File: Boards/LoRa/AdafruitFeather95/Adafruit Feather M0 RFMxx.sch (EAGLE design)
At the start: 38 parts, among them SW1 SPST_TACT-KMR2, U2 AP2112K-3.3, U3 MCP73831T-2ACI/OT, U4 RFM69HCW, X1 JSTPH, X2 32.768, X3 microUSB, X4 uFL

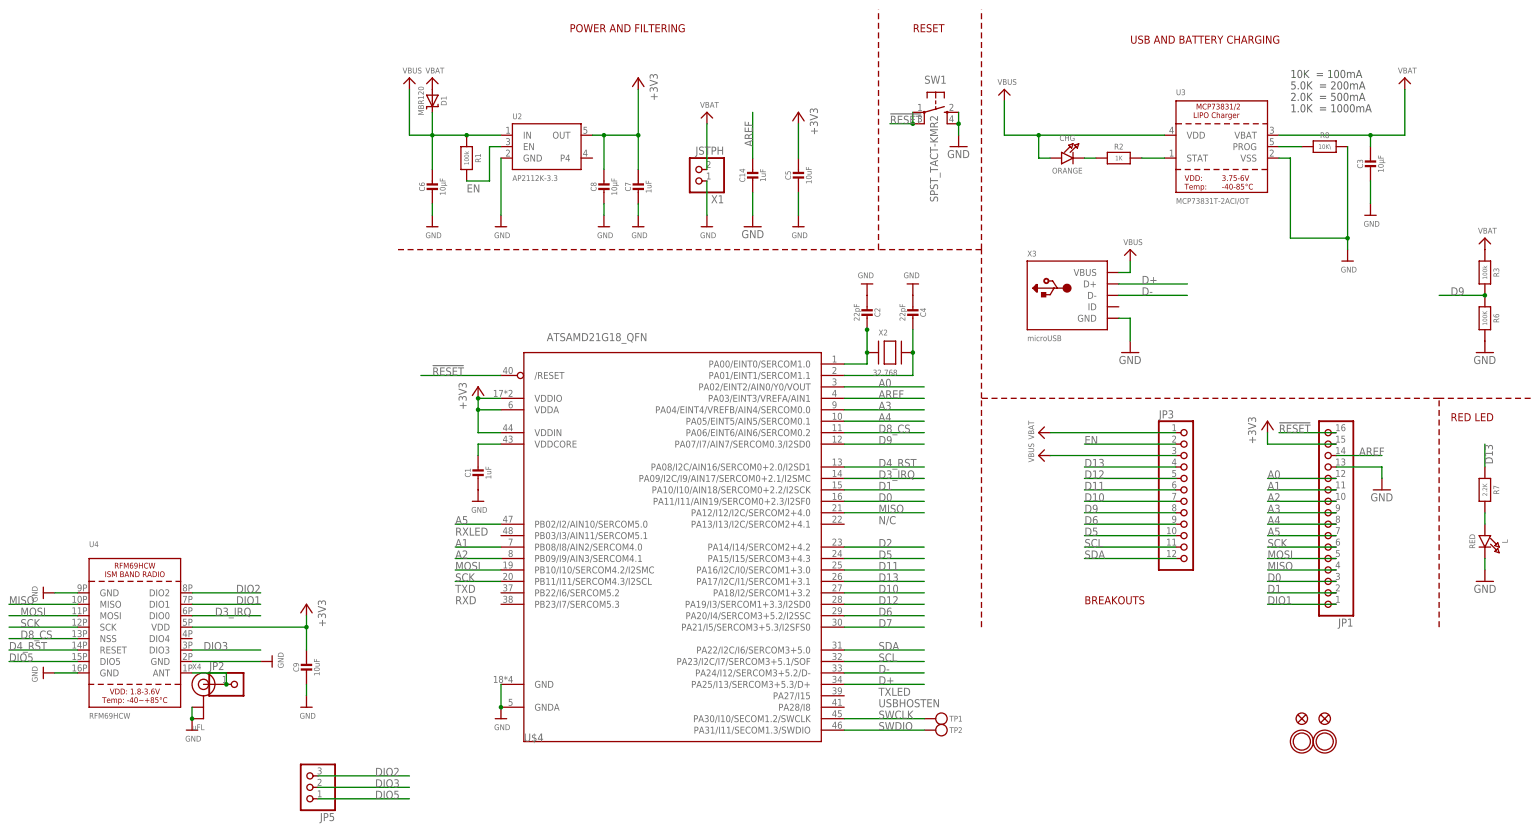
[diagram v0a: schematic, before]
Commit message: Cutting down the adafruit rfm board
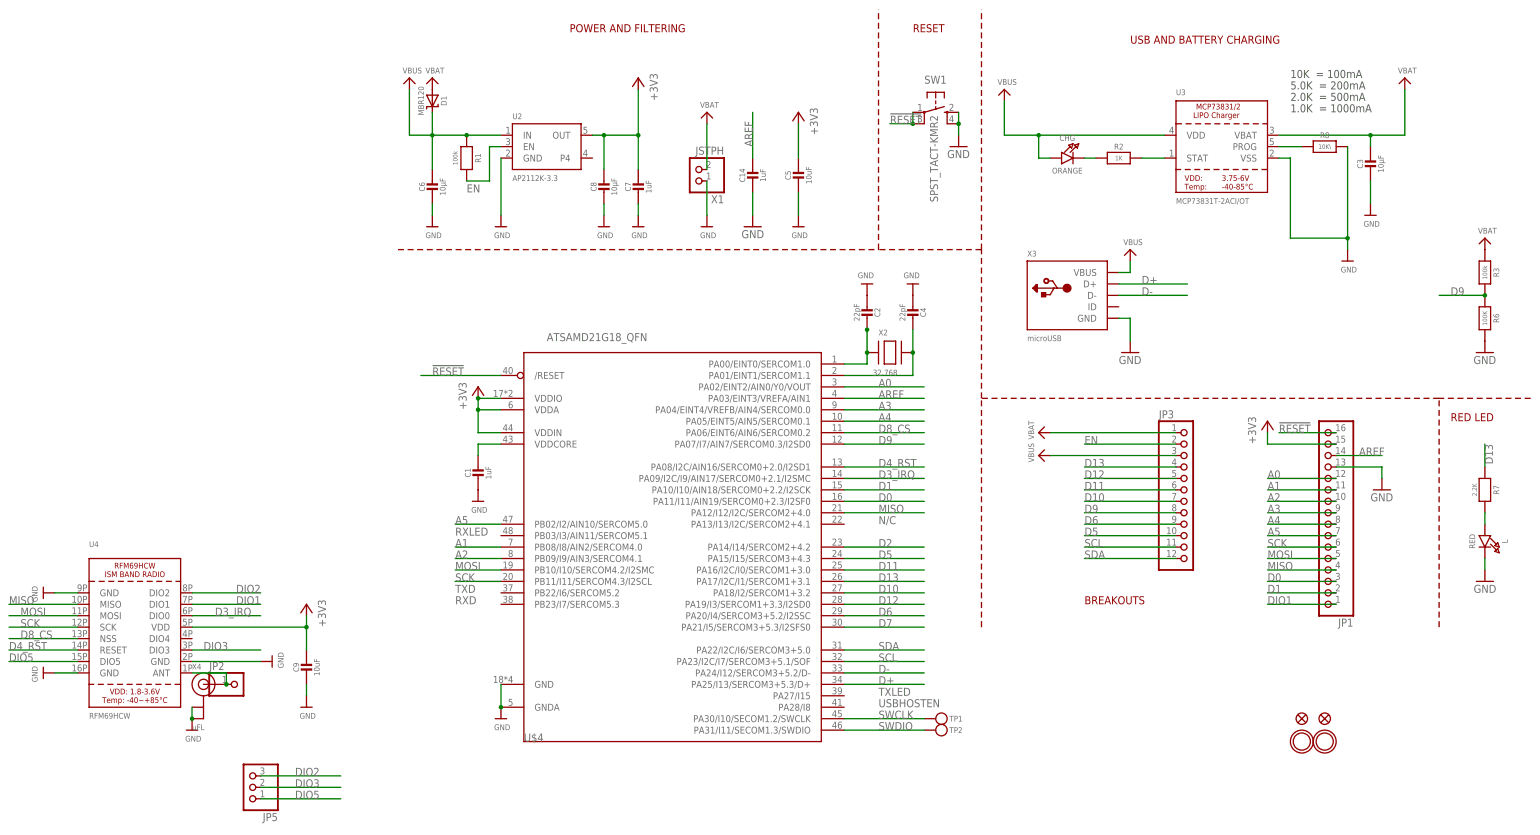
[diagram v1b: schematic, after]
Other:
- moved on the sheet: JP5
